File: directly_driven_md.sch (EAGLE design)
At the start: 23 parts, among them IC1 NJM2903D, IC2 LM78L12ACZ_NOPB, Q1 2SC1815_PBFREE, Q2 TTD1410B

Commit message: fixed L1 name
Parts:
- L1: value (none) -> MOTOR
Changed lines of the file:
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@@
 </classes>
 <parts>
-<part name="L1" library="rcl" library_urn="urn:adsk.eagle:library:334" deviceset="L-US" device="0207/15" package3d_urn="urn:adsk.eagle:package:23492/1"/>
+<part name="L1" library="rcl" library_urn="urn:adsk.eagle:library:334" deviceset="L-US" device="0207/15" package3d_urn="urn:adsk.eagle:package:23492/1" value="MOTOR"/>
 <part name="JP1" library="pinhead" library_urn="urn:adsk.eagle:library:325" deviceset="PINHD-1X2" device="" package3d_urn="urn:adsk.eagle:package:22435/2"/>
 <part name="GND1" library="supply1" library_urn="urn:adsk.eagle:library:371" deviceset="GND" device=""/>

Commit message: Fixed circuit
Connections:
- removed net N$25: C2.1, IC1.V+
- net +12V: now also C2.1, IC1.V+
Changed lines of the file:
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@@
 <part name="P+4" library="supply1" library_urn="urn:adsk.eagle:library:371" deviceset="+12V" device=""/>
 <part name="P+5" library="supply1" library_urn="urn:adsk.eagle:library:371" deviceset="+12V" device=""/>
+<part name="P+6" library="supply1" library_urn="urn:adsk.eagle:library:371" deviceset="+12V" device=""/>
 </parts>
 <sheets>
@@
 <instance part="P+5" gate="1" x="45.72" y="88.9" smashed="yes">
 <attribute name="VALUE" x="43.18" y="83.82" size="1.778" layer="96" rot="R90"/>
+</instance>
+<instance part="P+6" gate="1" x="22.86" y="88.9" smashed="yes">
+<attribute name="VALUE" x="20.32" y="83.82" size="1.778" layer="96" rot="R90"/>
 </instance>
 </instances>
@@
 <pinref part="P+5" gate="1" pin="+12V"/>
 </segment>
+<segment>
+<pinref part="IC1" gate="G$1" pin="V+"/>
+<wire x1="20.32" y1="63.5" x2="22.86" y2="63.5" width="0.1524" layer="91"/>
+<pinref part="C2" gate="G$1" pin="1"/>
+<wire x1="22.86" y1="63.5" x2="22.86" y2="38.1" width="0.1524" layer="91"/>
+<wire x1="22.86" y1="63.5" x2="22.86" y2="86.36" width="0.1524" layer="91"/>
+<junction x="22.86" y="63.5"/>
+<pinref part="P+6" gate="1" pin="+12V"/>
+</segment>
 </net>
 <net name="N$23" class="0">
@@
 </segment>
 </net>
-<net name="N$25" class="0">
-<segment>
-<pinref part="IC1" gate="G$1" pin="V+"/>
-<wire x1="20.32" y1="63.5" x2="22.86" y2="63.5" width="0.1524" layer="91"/>
-<pinref part="C2" gate="G$1" pin="1"/>
-<wire x1="22.86" y1="63.5" x2="22.86" y2="38.1" width="0.1524" layer="91"/>
-</segment>
-</net>

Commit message: fixed circuit
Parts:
- C3, C4: value (none) -> 220u
- C5: value 220u -> 47u
- R9: value 3.3 -> 3
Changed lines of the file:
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@@
 <part name="C2" library="rcl" library_urn="urn:adsk.eagle:library:334" deviceset="C-EU" device="025-025X050" package3d_urn="urn:adsk.eagle:package:23629/2" value="1u"/>
 <part name="R8" library="rcl" library_urn="urn:adsk.eagle:library:334" deviceset="R-EU_" device="0204/7" package3d_urn="urn:adsk.eagle:package:23498/2" value="3.3k"/>
-<part name="R9" library="rcl" library_urn="urn:adsk.eagle:library:334" deviceset="R-EU_" device="0204/7" package3d_urn="urn:adsk.eagle:package:23498/2" value="3.3"/>
+<part name="R9" library="rcl" library_urn="urn:adsk.eagle:library:334" deviceset="R-EU_" device="0204/7" package3d_urn="urn:adsk.eagle:package:23498/2" value="3"/>
 <part name="Q1" library="SamacSys_Parts" deviceset="2SC1815_PBFREE" device=""/>
 <part name="Q2" library="original" deviceset="TTD1410B" device=""/>
@@
 <part name="D3" library="SamacSys_Parts" deviceset="SB340LS" device=""/>
 <part name="P+1" library="supply1" library_urn="urn:adsk.eagle:library:371" deviceset="+12V" device=""/>
-<part name="C5" library="rcl" library_urn="urn:adsk.eagle:library:334" deviceset="CPOL-EU" device="E2,5-6E" package3d_urn="urn:adsk.eagle:package:23430/1" value="220u"/>
-<part name="C4" library="rcl" library_urn="urn:adsk.eagle:library:334" deviceset="C-EU" device="025-025X050" package3d_urn="urn:adsk.eagle:package:23629/2"/>
-<part name="C3" library="rcl" library_urn="urn:adsk.eagle:library:334" deviceset="C-EU" device="025-025X050" package3d_urn="urn:adsk.eagle:package:23629/2"/>
+<part name="C5" library="rcl" library_urn="urn:adsk.eagle:library:334" deviceset="CPOL-EU" device="E2,5-6E" package3d_urn="urn:adsk.eagle:package:23430/1" value="47u"/>
+<part name="C4" library="rcl" library_urn="urn:adsk.eagle:library:334" deviceset="C-EU" device="025-025X050" package3d_urn="urn:adsk.eagle:package:23629/2" value="220u"/>
+<part name="C3" library="rcl" library_urn="urn:adsk.eagle:library:334" deviceset="C-EU" device="025-025X050" package3d_urn="urn:adsk.eagle:package:23629/2" value="220u"/>
 <part name="GND2" library="supply1" library_urn="urn:adsk.eagle:library:371" deviceset="GND" device=""/>
 <part name="GND3" library="supply1" library_urn="urn:adsk.eagle:library:371" deviceset="GND" device=""/>

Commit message: circuit fixed
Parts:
- removed D3: SB340LS, SamacSys_Parts:SB340LS
- D2: value SB340LS -> ER504; device SamacSys_Parts:SB340LS -> SamacSys_Parts:ER504
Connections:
- removed net N$1: D2.A, D3.K
- net MOTOR: now also D2.A; no longer D3.A
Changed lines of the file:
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@@
 <part name="Q2" library="original" deviceset="TTD1410B" device=""/>
 <part name="D1" library="SamacSys_Parts" deviceset="1N4007GP-E3_54" device=""/>
-<part name="D2" library="SamacSys_Parts" deviceset="SB340LS" device=""/>
-<part name="D3" library="SamacSys_Parts" deviceset="SB340LS" device=""/>
 <part name="P+1" library="supply1" library_urn="urn:adsk.eagle:library:371" deviceset="+12V" device=""/>
 <part name="C5" library="rcl" library_urn="urn:adsk.eagle:library:334" deviceset="CPOL-EU" device="E2,5-6E" package3d_urn="urn:adsk.eagle:package:23430/1" value="47u"/>
@@
 <part name="P+5" library="supply1" library_urn="urn:adsk.eagle:library:371" deviceset="+12V" device=""/>
 <part name="P+6" library="supply1" library_urn="urn:adsk.eagle:library:371" deviceset="+12V" device=""/>
+<part name="D2" library="SamacSys_Parts" deviceset="ER504" device=""/>
 </parts>
 <sheets>
@@
 <attribute name="VALUE" x="15.24" y="29.21" size="1.778" layer="96" align="center-left"/>
 </instance>
-<instance part="D2" gate="G$1" x="68.58" y="68.58" smashed="yes" rot="R270">
-<attribute name="NAME" x="72.39" y="55.88" size="1.778" layer="95" rot="R270" align="center-left"/>
-<attribute name="VALUE" x="62.23" y="63.5" size="1.778" layer="96" rot="R270" align="center-left"/>
-</instance>
-<instance part="D3" gate="G$1" x="68.58" y="53.34" smashed="yes" rot="R270">
-<attribute name="NAME" x="72.39" y="40.64" size="1.778" layer="95" rot="R270" align="center-left"/>
-<attribute name="VALUE" x="62.23" y="48.26" size="1.778" layer="96" rot="R270" align="center-left"/>
-</instance>
 <instance part="P+1" gate="1" x="40.64" y="63.5" smashed="yes">
 <attribute name="VALUE" x="45.72" y="58.42" size="1.778" layer="96" rot="R90"/>
@@
 <instance part="GND2" gate="1" x="40.64" y="20.32" smashed="yes">
 <attribute name="VALUE" x="38.1" y="17.78" size="1.778" layer="96"/>
+</instance>
+<instance part="D2" gate="G$1" x="68.58" y="58.42" smashed="yes" rot="R270">
+<attribute name="NAME" x="73.66" y="46.99" size="1.778" layer="95" rot="R270" align="center-left"/>
+<attribute name="VALUE" x="71.12" y="46.99" size="1.778" layer="96" rot="R270" align="center-left"/>
 </instance>
 </instances>
@@
 <wire x1="78.74" y1="33.02" x2="68.58" y2="33.02" width="0.1524" layer="91"/>
 <label x="81.28" y="35.56" size="1.778" layer="95"/>
-<pinref part="D3" gate="G$1" pin="A"/>
-<wire x1="68.58" y1="35.56" x2="68.58" y2="33.02" width="0.1524" layer="91"/>
 <wire x1="78.74" y1="33.02" x2="83.82" y2="33.02" width="0.1524" layer="91"/>
 <junction x="78.74" y="33.02"/>
+<pinref part="D2" gate="G$1" pin="A"/>
+<wire x1="68.58" y1="43.18" x2="68.58" y2="33.02" width="0.1524" layer="91"/>
 </segment>
 </net>
@@
 <wire x1="7.62" y1="58.42" x2="0" y2="58.42" width="0.1524" layer="91"/>
 <pinref part="L1" gate="G$1" pin="1"/>
-<wire x1="68.58" y1="68.58" x2="78.74" y2="68.58" width="0.1524" layer="91"/>
 <wire x1="78.74" y1="68.58" x2="78.74" y2="58.42" width="0.1524" layer="91"/>
-<pinref part="D2" gate="G$1" pin="K"/>
-<wire x1="68.58" y1="68.58" x2="68.58" y2="66.04" width="0.1524" layer="91"/>
 <wire x1="7.62" y1="68.58" x2="15.24" y2="68.58" width="0.1524" layer="91"/>
-<junction x="68.58" y="68.58"/>
 <pinref part="IC2" gate="G$1" pin="VIN"/>
 <wire x1="15.24" y1="68.58" x2="22.86" y2="68.58" width="0.1524" layer="91"/>
 <wire x1="22.86" y1="68.58" x2="38.1" y2="68.58" width="0.1524" layer="91"/>
 <wire x1="38.1" y1="68.58" x2="68.58" y2="68.58" width="0.1524" layer="91"/>
+<wire x1="68.58" y1="68.58" x2="78.74" y2="68.58" width="0.1524" layer="91"/>
 <wire x1="38.1" y1="55.88" x2="38.1" y2="68.58" width="0.1524" layer="91"/>
 <junction x="38.1" y="68.58"/>
@@
 <wire x1="22.86" y1="60.96" x2="22.86" y2="68.58" width="0.1524" layer="91"/>
 <junction x="22.86" y="68.58"/>
-</segment>
-</net>
-<net name="N$1" class="0">
-<segment>
-<pinref part="D2" gate="G$1" pin="A"/>
-<pinref part="D3" gate="G$1" pin="K"/>
-</segment>
-</net>
+<pinref part="D2" gate="G$1" pin="K"/>
+<wire x1="68.58" y1="58.42" x2="68.58" y2="68.58" width="0.1524" layer="91"/>
+<junction x="68.58" y="68.58"/>
+</segment>
+</net>

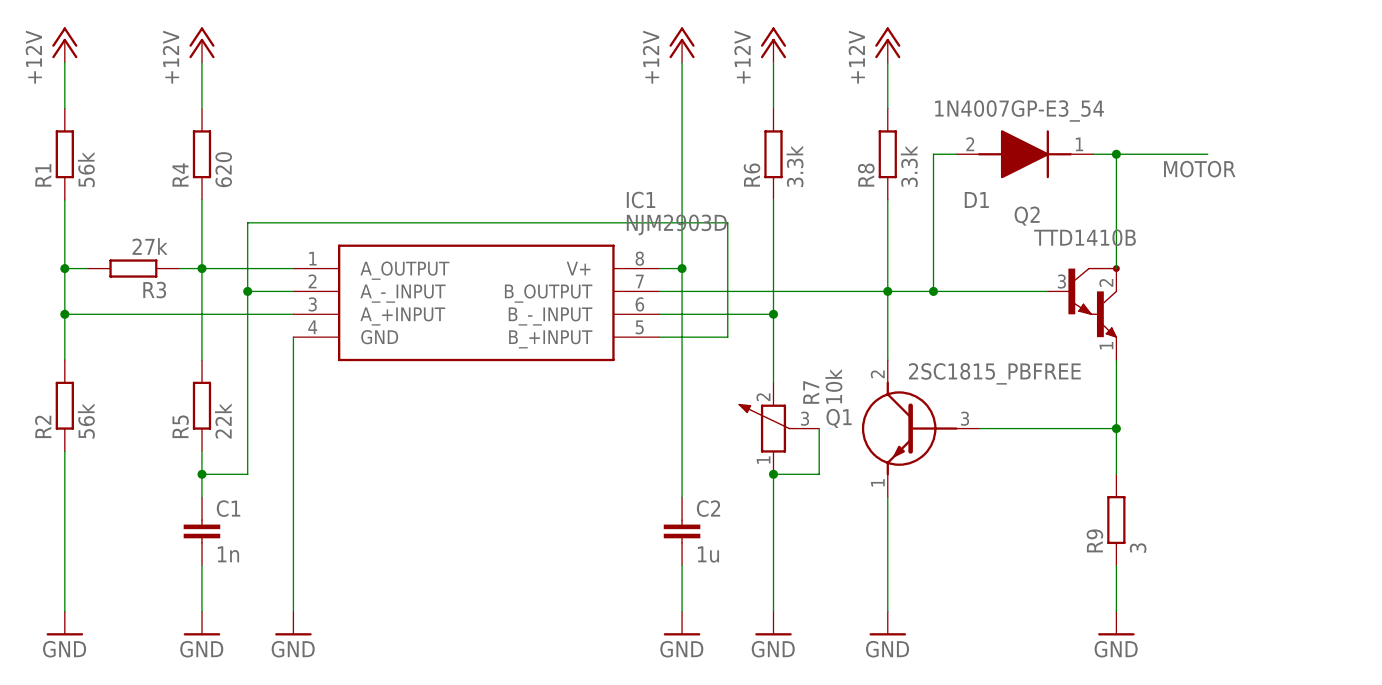
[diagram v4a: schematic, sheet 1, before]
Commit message: switch is added
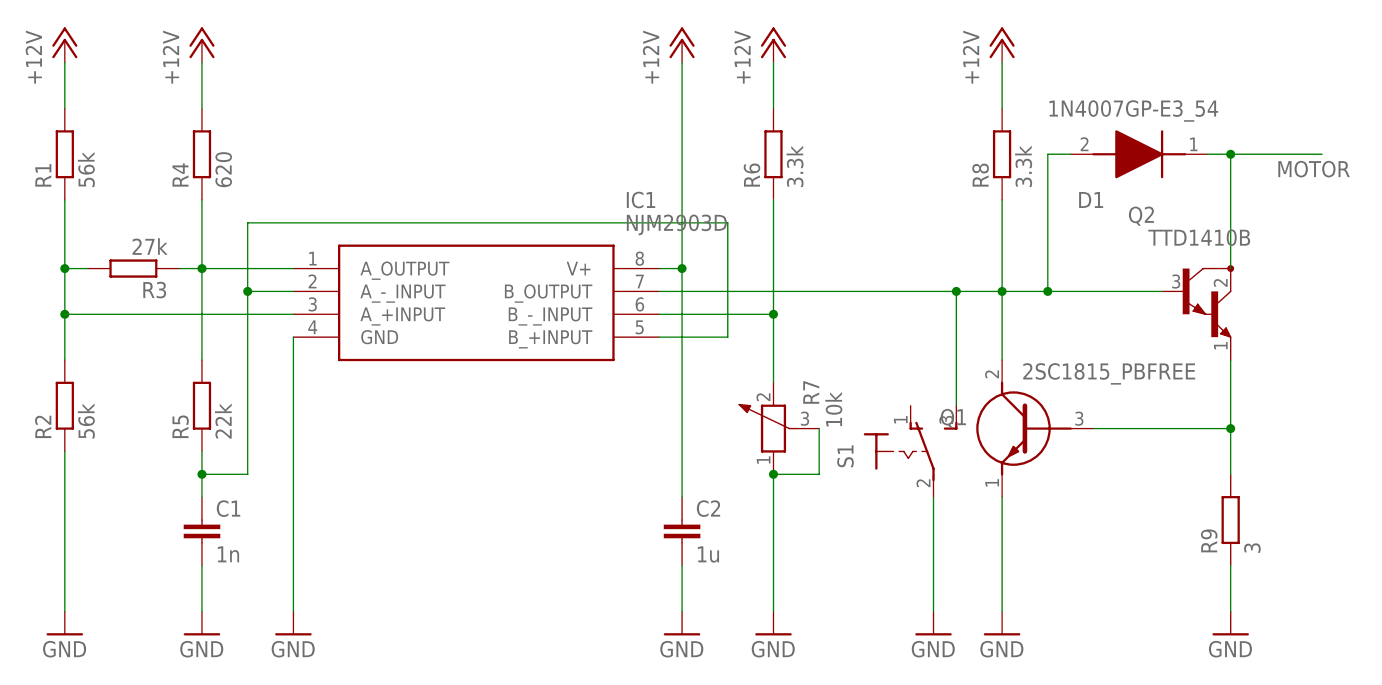
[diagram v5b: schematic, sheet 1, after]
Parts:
- added S1: (no value), switch:320-916
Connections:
- net GND: now also S1.P
- net N$23: now also S1.S
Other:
- moved on the sheet: D1, Q1, Q2, R8, R9
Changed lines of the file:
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@@
 <part name="P+6" library="supply1" library_urn="urn:adsk.eagle:library:371" deviceset="+12V" device=""/>
 <part name="D2" library="SamacSys_Parts" deviceset="ER504" device=""/>
+<part name="S1" library="switch" library_urn="urn:adsk.eagle:library:380" deviceset="320-916" device="" package3d_urn="urn:adsk.eagle:package:27678/1"/>
+<part name="GND10" library="supply1" library_urn="urn:adsk.eagle:library:371" deviceset="GND" device=""/>
 </parts>
 <sheets>
@@
 <instance part="R7" gate="1" x="33.02" y="45.72" smashed="yes" rot="R90">
 <attribute name="NAME" x="38.1" y="48.26" size="1.778" layer="95" rot="R90"/>
-<attribute name="VALUE" x="40.64" y="48.26" size="1.778" layer="96" rot="R90"/>
+<attribute name="VALUE" x="40.64" y="45.72" size="1.778" layer="96" rot="R90"/>
 </instance>
 <instance part="C2" gate="G$1" x="22.86" y="35.56" smashed="yes">
@@
 <attribute name="VALUE" x="24.384" y="30.861" size="1.778" layer="96"/>
 </instance>
-<instance part="R8" gate="G$1" x="45.72" y="76.2" smashed="yes" rot="R90">
-<attribute name="NAME" x="44.2214" y="72.39" size="1.778" layer="95" rot="R90"/>
-<attribute name="VALUE" x="49.022" y="72.39" size="1.778" layer="96" rot="R90"/>
-</instance>
-<instance part="R9" gate="G$1" x="71.12" y="35.56" smashed="yes" rot="R90">
-<attribute name="NAME" x="69.6214" y="31.75" size="1.778" layer="95" rot="R90"/>
-<attribute name="VALUE" x="74.422" y="31.75" size="1.778" layer="96" rot="R90"/>
-</instance>
-<instance part="Q1" gate="G$1" x="55.88" y="45.72" smashed="yes" rot="MR0">
-<attribute name="NAME" x="41.91" y="46.99" size="1.778" layer="95" rot="MR0" align="center-left"/>
-<attribute name="VALUE" x="67.31" y="52.07" size="1.778" layer="96" rot="MR0" align="center-left"/>
-</instance>
-<instance part="Q2" gate="G$1" x="66.04" y="60.96" smashed="yes">
-<attribute name="NAME" x="59.69" y="68.58" size="1.778" layer="95"/>
-<attribute name="VALUE" x="61.976" y="66.04" size="1.778" layer="96"/>
-</instance>
-<instance part="D1" gate="G$1" x="68.58" y="76.2" smashed="yes" rot="R180">
-<attribute name="NAME" x="57.15" y="71.12" size="1.778" layer="95" rot="R180" align="center-left"/>
-<attribute name="VALUE" x="69.85" y="81.28" size="1.778" layer="96" rot="R180" align="center-left"/>
+<instance part="R8" gate="G$1" x="58.42" y="76.2" smashed="yes" rot="R90">
+<attribute name="NAME" x="56.9214" y="72.39" size="1.778" layer="95" rot="R90"/>
+<attribute name="VALUE" x="61.722" y="72.39" size="1.778" layer="96" rot="R90"/>
+</instance>
+<instance part="R9" gate="G$1" x="83.82" y="35.56" smashed="yes" rot="R90">
+<attribute name="NAME" x="82.3214" y="31.75" size="1.778" layer="95" rot="R90"/>
+<attribute name="VALUE" x="87.122" y="31.75" size="1.778" layer="96" rot="R90"/>
+</instance>
+<instance part="Q1" gate="G$1" x="68.58" y="45.72" smashed="yes" rot="MR0">
+<attribute name="NAME" x="54.61" y="46.99" size="1.778" layer="95" rot="MR0" align="center-left"/>
+<attribute name="VALUE" x="80.01" y="52.07" size="1.778" layer="96" rot="MR0" align="center-left"/>
+</instance>
+<instance part="Q2" gate="G$1" x="78.74" y="60.96" smashed="yes">
+<attribute name="NAME" x="72.39" y="68.58" size="1.778" layer="95"/>
+<attribute name="VALUE" x="74.676" y="66.04" size="1.778" layer="96"/>
+</instance>
+<instance part="D1" gate="G$1" x="81.28" y="76.2" smashed="yes" rot="R180">
+<attribute name="NAME" x="69.85" y="71.12" size="1.778" layer="95" rot="R180" align="center-left"/>
+<attribute name="VALUE" x="82.55" y="81.28" size="1.778" layer="96" rot="R180" align="center-left"/>
 </instance>
 <instance part="GND3" gate="1" x="-45.72" y="22.86" smashed="yes">
@@
 <attribute name="VALUE" x="30.48" y="20.32" size="1.778" layer="96"/>
 </instance>
-<instance part="GND8" gate="1" x="45.72" y="22.86" smashed="yes">
-<attribute name="VALUE" x="43.18" y="20.32" size="1.778" layer="96"/>
-</instance>
-<instance part="GND9" gate="1" x="71.12" y="22.86" smashed="yes">
-<attribute name="VALUE" x="68.58" y="20.32" size="1.778" layer="96"/>
+<instance part="GND8" gate="1" x="58.42" y="22.86" smashed="yes">
+<attribute name="VALUE" x="55.88" y="20.32" size="1.778" layer="96"/>
+</instance>
+<instance part="GND9" gate="1" x="83.82" y="22.86" smashed="yes">
+<attribute name="VALUE" x="81.28" y="20.32" size="1.778" layer="96"/>
 </instance>
 <instance part="P+2" gate="1" x="-45.72" y="88.9" smashed="yes">
@@
 <attribute name="VALUE" x="30.48" y="83.82" size="1.778" layer="96" rot="R90"/>
 </instance>
-<instance part="P+5" gate="1" x="45.72" y="88.9" smashed="yes">
-<attribute name="VALUE" x="43.18" y="83.82" size="1.778" layer="96" rot="R90"/>
+<instance part="P+5" gate="1" x="58.42" y="88.9" smashed="yes">
+<attribute name="VALUE" x="55.88" y="83.82" size="1.778" layer="96" rot="R90"/>
 </instance>
 <instance part="P+6" gate="1" x="22.86" y="88.9" smashed="yes">
 <attribute name="VALUE" x="20.32" y="83.82" size="1.778" layer="96" rot="R90"/>
+</instance>
+<instance part="S1" gate="1" x="48.26" y="43.18" smashed="yes">
+<attribute name="NAME" x="41.91" y="41.275" size="1.778" layer="95" rot="R90"/>
+<attribute name="VALUE" x="44.45" y="45.72" size="1.778" layer="96" rot="R90"/>
+</instance>
+<instance part="GND10" gate="1" x="50.8" y="22.86" smashed="yes">
+<attribute name="VALUE" x="48.26" y="20.32" size="1.778" layer="96"/>
 </instance>
 </instances>
@@
 <segment>
 <pinref part="Q1" gate="G$1" pin="E"/>
-<wire x1="45.72" y1="38.1" x2="45.72" y2="25.4" width="0.1524" layer="91"/>
+<wire x1="58.42" y1="38.1" x2="58.42" y2="25.4" width="0.1524" layer="91"/>
 <pinref part="GND8" gate="1" pin="GND"/>
 </segment>
 <segment>
 <pinref part="R9" gate="G$1" pin="1"/>
-<wire x1="71.12" y1="30.48" x2="71.12" y2="25.4" width="0.1524" layer="91"/>
+<wire x1="83.82" y1="30.48" x2="83.82" y2="25.4" width="0.1524" layer="91"/>
 <pinref part="GND9" gate="1" pin="GND"/>
+</segment>
+<segment>
+<pinref part="S1" gate="1" pin="P"/>
+<wire x1="50.8" y1="38.1" x2="50.8" y2="25.4" width="0.1524" layer="91"/>
+<pinref part="GND10" gate="1" pin="GND"/>
 </segment>
 </net>
@@
 <segment>
 <pinref part="R8" gate="G$1" pin="2"/>
-<wire x1="45.72" y1="81.28" x2="45.72" y2="86.36" width="0.1524" layer="91"/>
+<wire x1="58.42" y1="81.28" x2="58.42" y2="86.36" width="0.1524" layer="91"/>
 <pinref part="P+5" gate="1" pin="+12V"/>
 </segment>
@@
 <pinref part="Q2" gate="G$1" pin="B"/>
 <pinref part="R8" gate="G$1" pin="1"/>
-<wire x1="45.72" y1="60.96" x2="50.8" y2="60.96" width="0.1524" layer="91"/>
-<wire x1="50.8" y1="60.96" x2="63.5" y2="60.96" width="0.1524" layer="91"/>
-<wire x1="45.72" y1="71.12" x2="45.72" y2="60.96" width="0.1524" layer="91"/>
-<junction x="45.72" y="60.96"/>
+<wire x1="58.42" y1="60.96" x2="63.5" y2="60.96" width="0.1524" layer="91"/>
+<wire x1="63.5" y1="60.96" x2="76.2" y2="60.96" width="0.1524" layer="91"/>
+<wire x1="58.42" y1="71.12" x2="58.42" y2="60.96" width="0.1524" layer="91"/>
+<junction x="58.42" y="60.96"/>
 <pinref part="Q1" gate="G$1" pin="C"/>
-<wire x1="45.72" y1="60.96" x2="45.72" y2="53.34" width="0.1524" layer="91"/>
+<wire x1="58.42" y1="60.96" x2="58.42" y2="53.34" width="0.1524" layer="91"/>
 <pinref part="D1" gate="G$1" pin="A"/>
-<wire x1="53.34" y1="76.2" x2="50.8" y2="76.2" width="0.1524" layer="91"/>
-<wire x1="50.8" y1="76.2" x2="50.8" y2="60.96" width="0.1524" layer="91"/>
-<junction x="50.8" y="60.96"/>
+<wire x1="66.04" y1="76.2" x2="63.5" y2="76.2" width="0.1524" layer="91"/>
+<wire x1="63.5" y1="76.2" x2="63.5" y2="60.96" width="0.1524" layer="91"/>
+<junction x="63.5" y="60.96"/>
 <pinref part="IC1" gate="G$1" pin="B_OUTPUT"/>
-<wire x1="20.32" y1="60.96" x2="45.72" y2="60.96" width="0.1524" layer="91"/>
+<wire x1="20.32" y1="60.96" x2="53.34" y2="60.96" width="0.1524" layer="91"/>
+<pinref part="S1" gate="1" pin="S"/>
+<wire x1="53.34" y1="60.96" x2="58.42" y2="60.96" width="0.1524" layer="91"/>
+<wire x1="53.34" y1="48.26" x2="53.34" y2="60.96" width="0.1524" layer="91"/>
+<junction x="53.34" y="60.96"/>
 </segment>
 </net>
@@
 <pinref part="Q2" gate="G$1" pin="E"/>
 <pinref part="R9" gate="G$1" pin="2"/>
-<wire x1="71.12" y1="53.34" x2="71.12" y2="45.72" width="0.1524" layer="91"/>
+<wire x1="83.82" y1="53.34" x2="83.82" y2="45.72" width="0.1524" layer="91"/>
 <pinref part="Q1" gate="G$1" pin="B"/>
-<wire x1="71.12" y1="45.72" x2="71.12" y2="40.64" width="0.1524" layer="91"/>
-<wire x1="55.88" y1="45.72" x2="71.12" y2="45.72" width="0.1524" layer="91"/>
-<junction x="71.12" y="45.72"/>
+<wire x1="83.82" y1="45.72" x2="83.82" y2="40.64" width="0.1524" layer="91"/>
+<wire x1="68.58" y1="45.72" x2="83.82" y2="45.72" width="0.1524" layer="91"/>
+<junction x="83.82" y="45.72"/>
 </segment>
 </net>
@@
 <segment>
 <pinref part="Q2" gate="G$1" pin="C"/>
-<wire x1="71.12" y1="63.5" x2="71.12" y2="76.2" width="0.1524" layer="91"/>
-<wire x1="71.12" y1="76.2" x2="81.28" y2="76.2" width="0.1524" layer="91"/>
+<wire x1="83.82" y1="63.5" x2="83.82" y2="76.2" width="0.1524" layer="91"/>
+<wire x1="83.82" y1="76.2" x2="93.98" y2="76.2" width="0.1524" layer="91"/>
 <pinref part="D1" gate="G$1" pin="K"/>
-<wire x1="68.58" y1="76.2" x2="71.12" y2="76.2" width="0.1524" layer="91"/>
-<junction x="71.12" y="76.2"/>
-<label x="76.2" y="73.66" size="1.778" layer="95"/>
-</segment>
-</net>
+<wire x1="81.28" y1="76.2" x2="83.82" y2="76.2" width="0.1524" layer="91"/>
+<junction x="83.82" y="76.2"/>
+<label x="88.9" y="73.66" size="1.778" layer="95"/>
+</segment>
+</net>
